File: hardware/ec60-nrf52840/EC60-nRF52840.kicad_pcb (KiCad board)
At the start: 4 copper layers, 285 x 94.6 mm, 180 parts, among them J1 REAR_USB_DAUGHTERBOARD, J2 PROTECTED_1S_4V2_NTC10K, J3 SWD_POGO, SW1 EVQPUC02K_RESET, SW10 EC_SW, SW100 JS102011SAQN_POWER, SW11 EC_SW, SW12 EC_SW, SW13 EC_SW, SW14 EC_SW, SW15 EC_SW, SW16 EC_SW, SW17 EC_SW, SW18 EC_SW, SW19 EC_SW, SW2 EC_SW, SW20 EC_SW, SW21 EC_SW, SW22 EC_SW, SW23 EC_SW, SW24 EC_SW, SW25 EC_SW, SW26 EC_SW, SW27 EC_SW, SW28 EC_SW, SW29 EC_SW, SW3 EC_SW, SW30 EC_SW, SW31 ANSI_\, SW32 ISO_Enter, SW33 EC_SW, SW34 EC_SW, SW35 EC_SW, SW36 EC_SW, SW37 EC_SW, SW38 EC_SW, SW39 EC_SW, SW4 EC_SW, SW40 EC_SW, SW41 EC_SW, SW42 EC_SW, SW43 EC_SW, SW44 EC_SW, SW45 ISO_|, SW46 ANSI_Enter, SW47 EC_SW, SW48 EC_SW, SW49 EC_SW, SW5 EC_SW, SW50 EC_SW, SW51 EC_SW, SW52 EC_SW, SW53 EC_SW, SW54 EC_SW, SW55 EC_SW, SW56 EC_SW, SW57 EC_SW, SW58 EC_SW, SW59 EC_SW, SW6 EC_SW, SW60 EC_SW_1u&1.75u, SW61 EC_SW, SW62 EC_SW_1u&1.75u, SW63 EC_SW, SW64 EC_SW, SW65 EC_SW, SW66 EC_SW, SW67 EC_SW, SW68 EC_SW, SW69 EC_SW, SW7 EC_SW, SW70 EC_SW, SW71 EC_SW, SW72 EC_SW, SW73 EC_SW, SW74 EC_SW, SW75 EC_SW, SW8 EC_SW, SW9 EC_SW, U1 MDBT50Q-1MV2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

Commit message: fix: validate single-nRF PCB and add 3D renders
Complete routing and native clearance repairs, freeze footprint metadata, and preserve EC60 sensing and mounting geometry. Add reproducible KiCad stills and a six-second 3D turntable with model provenance.

Validation: strict DRC 0 errors and 0 opens; ERC 0 errors; 268 physical pin pairs pass with no connectivity regressions. Render source hashes are unchanged, and MP4/GIF decoding passes. Physical assembly and SI/RF validation remain pending.
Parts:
- removed G*** (x3): LOGO, LOGO
- C10: footprint Capacitor_SMD:C_0402_1005Metric -> YAECKB:C_0402_1005Metric__C10
- C11: footprint Capacitor_SMD:C_0402_1005Metric -> YAECKB:C_0402_1005Metric__C11
- C12: footprint Capacitor_SMD:C_0402_1005Metric -> YAECKB:C_0402_1005Metric__C12
- C13: footprint Capacitor_SMD:C_0402_1005Metric -> YAECKB:C_0402_1005Metric__C13
- C30: footprint Capacitor_SMD:C_0603_1608Metric -> YAECKB:C_0603_1608Metric__C30
- C31: footprint Capacitor_SMD:C_0402_1005Metric -> YAECKB:C_0402_1005Metric__C31
- C32: footprint Capacitor_SMD:C_0603_1608Metric -> YAECKB:C_0603_1608Metric__C32
- C40: footprint Capacitor_SMD:C_0603_1608Metric -> YAECKB:C_0603_1608Metric__C40
- C41: footprint Capacitor_SMD:C_0603_1608Metric -> YAECKB:C_0603_1608Metric__C41
- C42: footprint Capacitor_SMD:C_0603_1608Metric -> YAECKB:C_0603_1608Metric__C42
- C43: footprint Capacitor_SMD:C_0603_1608Metric -> YAECKB:C_0603_1608Metric__C43
- C44: footprint Capacitor_SMD:C_0603_1608Metric -> YAECKB:C_0603_1608Metric__C44
- C45: footprint Capacitor_SMD:C_0603_1608Metric -> YAECKB:C_0603_1608Metric__C45
- C46: footprint Capacitor_SMD:C_0603_1608Metric -> YAECKB:C_0603_1608Metric__C46
- C47: footprint Capacitor_SMD:C_0402_1005Metric -> YAECKB:C_0402_1005Metric__C47
- C48: footprint Capacitor_SMD:C_0402_1005Metric -> YAECKB:C_0402_1005Metric__C48
- C9: footprint Capacitor_SMD:C_0402_1005Metric -> YAECKB:C_0402_1005Metric__C9
- D1: footprint Package_TO_SOT_SMD:SOT-143 -> YAECKB:SOT-143__D1
- D2: footprint LED_SMD:LED_0603_1608Metric -> YAECKB:LED_0603_1608Metric__D2
- F1: footprint Fuse:Fuse_1206_3216Metric -> YAECKB:Fuse_1206_3216Metric__F1
- H1: footprint YAECKB:HOLE_M2 -> YAECKB:HOLE_M2__H1
- H10: footprint YAECKB:HOLE_M2 -> YAECKB:HOLE_M2__H10
- H11: footprint YAECKB:HOLE_M2 -> YAECKB:HOLE_M2__H11
- H12: footprint YAECKB:HOLE_M2 -> YAECKB:HOLE_M2__H12
- H13: footprint YAECKB:HOLE_M2 -> YAECKB:HOLE_M2__H13
- H14: footprint YAECKB:HOLE_M2 -> YAECKB:HOLE_M2__H14
- H15: footprint YAECKB:HOLE_M2 -> YAECKB:HOLE_M2__H15
- H16: footprint YAECKB:HOLE_M2 -> YAECKB:HOLE_M2__H16
- H17: footprint YAECKB:HOLE_M2 -> YAECKB:HOLE_M2__H17
- H18: footprint YAECKB:HOLE_M2 -> YAECKB:HOLE_M2__H18
- H19: footprint YAECKB:HOLE_M2 -> YAECKB:HOLE_M2__H19
- H2: footprint YAECKB:HOLE_M2 -> YAECKB:HOLE_M2__H2
- H20: footprint YAECKB:HOLE_M2 -> YAECKB:HOLE_M2__H20
- H21: footprint YAECKB:HOLE_M2 -> YAECKB:HOLE_M2__H21
- H22: footprint YAECKB:HOLE_M2 -> YAECKB:HOLE_M2__H22
- H23: footprint YAECKB:HOLE_M2 -> YAECKB:HOLE_M2__H23
- H24: footprint YAECKB:HOLE_M2 -> YAECKB:HOLE_M2__H24
- H25: footprint YAECKB:HOLE_M2 -> YAECKB:HOLE_M2__H25
- H26: footprint YAECKB:HOLE_M2 -> YAECKB:HOLE_M2__H26
- H3: footprint YAECKB:HOLE_M2 -> YAECKB:HOLE_M2__H3
- H4: footprint YAECKB:HOLE_M2 -> YAECKB:HOLE_M2__H4
- H5: footprint YAECKB:HOLE_M2 -> YAECKB:HOLE_M2__H5
- H6: footprint YAECKB:HOLE_M2 -> YAECKB:HOLE_M2__H6
- H7: footprint YAECKB:HOLE_M2 -> YAECKB:HOLE_M2__H7
- H8: footprint YAECKB:HOLE_M2 -> YAECKB:HOLE_M2__H8
- H9: footprint YAECKB:HOLE_M2 -> YAECKB:HOLE_M2__H9
- J1: footprint YAECKB:JST-SR-4 -> YAECKB:JST-SR-4__J1
- J2: footprint Connector_JST:JST_PH_S3B-PH-SM4-TB_1x03-1MP_P2.00mm_Horizontal -> YAECKB:JST_PH_S3B-PH-SM4-TB_1x03-1MP_P2.00mm_Horizontal__J2
- J3: footprint YAECKB:SWD_Pogo_2x03 -> YAECKB:SWD_Pogo_2x03__J3
- JP1: footprint Resistor_SMD:R_0603_1608Metric_Pad0.98x0.95mm_HandSolder -> YAECKB:R_0603_1608Metric_Pad0.98x0.95mm_HandSolder__JP1
- L1: footprint Inductor_SMD:L_Wuerth_MAPI-3015 -> YAECKB:L_Wuerth_MAPI-3015__L1
- R10: footprint Resistor_SMD:R_0402_1005Metric -> YAECKB:R_0402_1005Metric__R10
- R11: footprint Resistor_SMD:R_0402_1005Metric -> YAECKB:R_0402_1005Metric__R11
- R12: footprint Resistor_SMD:R_0402_1005Metric -> YAECKB:R_0402_1005Metric__R12
- R13: footprint Resistor_SMD:R_0402_1005Metric -> YAECKB:R_0402_1005Metric__R13
- R14: footprint Resistor_SMD:R_0402_1005Metric -> YAECKB:R_0402_1005Metric__R14
- R15: footprint Resistor_SMD:R_0402_1005Metric -> YAECKB:R_0402_1005Metric__R15
- R16: footprint Resistor_SMD:R_0402_1005Metric -> YAECKB:R_0402_1005Metric__R16
- R17: footprint Resistor_SMD:R_0402_1005Metric -> YAECKB:R_0402_1005Metric__R17
- R18: footprint Resistor_SMD:R_0402_1005Metric -> YAECKB:R_0402_1005Metric__R18
- R19: footprint Resistor_SMD:R_0402_1005Metric -> YAECKB:R_0402_1005Metric__R19
- R20: footprint Resistor_SMD:R_0402_1005Metric -> YAECKB:R_0402_1005Metric__R20
- R21: footprint Resistor_SMD:R_0402_1005Metric -> YAECKB:R_0402_1005Metric__R21
- R23: footprint Resistor_SMD:R_0402_1005Metric -> YAECKB:R_0402_1005Metric__R23
- R24: footprint Resistor_SMD:R_0402_1005Metric -> YAECKB:R_0402_1005Metric__R24
- R25: footprint Resistor_SMD:R_0402_1005Metric -> YAECKB:R_0402_1005Metric__R25
- R26: footprint Resistor_SMD:R_0402_1005Metric -> YAECKB:R_0402_1005Metric__R26
- R3: footprint Resistor_SMD:R_0402_1005Metric -> YAECKB:R_0402_1005Metric__R3
- R30: footprint Resistor_SMD:R_0402_1005Metric -> YAECKB:R_0402_1005Metric__R30
- R31: footprint Resistor_SMD:R_0402_1005Metric -> YAECKB:R_0402_1005Metric__R31
- R32: footprint Resistor_SMD:R_0402_1005Metric -> YAECKB:R_0402_1005Metric__R32
- R4: footprint Resistor_SMD:R_0402_1005Metric -> YAECKB:R_0402_1005Metric__R4
- R40: footprint Resistor_SMD:R_0402_1005Metric -> YAECKB:R_0402_1005Metric__R40
- R41: footprint Resistor_SMD:R_0402_1005Metric -> YAECKB:R_0402_1005Metric__R41
- R42: footprint Resistor_SMD:R_0402_1005Metric -> YAECKB:R_0402_1005Metric__R42
- R43: footprint Resistor_SMD:R_0402_1005Metric -> YAECKB:R_0402_1005Metric__R43
- R44: footprint Resistor_SMD:R_0402_1005Metric -> YAECKB:R_0402_1005Metric__R44
- R45: footprint Resistor_SMD:R_0402_1005Metric -> YAECKB:R_0402_1005Metric__R45
- R46: footprint Resistor_SMD:R_0402_1005Metric -> YAECKB:R_0402_1005Metric__R46
- R47: footprint Resistor_SMD:R_0402_1005Metric -> YAECKB:R_0402_1005Metric__R47
- R48: footprint Resistor_SMD:R_0402_1005Metric -> YAECKB:R_0402_1005Metric__R48
- R49: footprint Resistor_SMD:R_0402_1005Metric -> YAECKB:R_0402_1005Metric__R49
- R5: footprint Resistor_SMD:R_0402_1005Metric -> YAECKB:R_0402_1005Metric__R5
- R50: footprint Resistor_SMD:R_0402_1005Metric -> YAECKB:R_0402_1005Metric__R50
- R51: footprint Resistor_SMD:R_0402_1005Metric -> YAECKB:R_0402_1005Metric__R51
- R52: footprint Resistor_SMD:R_0402_1005Metric -> YAECKB:R_0402_1005Metric__R52
- R53: footprint Resistor_SMD:R_0402_1005Metric -> YAECKB:R_0402_1005Metric__R53
- R54: footprint Resistor_SMD:R_0402_1005Metric -> YAECKB:R_0402_1005Metric__R54
- R6: footprint Resistor_SMD:R_0402_1005Metric -> YAECKB:R_0402_1005Metric__R6
- R7: footprint Resistor_SMD:R_0402_1005Metric -> YAECKB:R_0402_1005Metric__R7
- R8: footprint Resistor_SMD:R_0402_1005Metric -> YAECKB:R_0402_1005Metric__R8
- R9: footprint Resistor_SMD:R_0402_1005Metric -> YAECKB:R_0402_1005Metric__R9
- REF**: footprint locallib:60_Outline-Modded-Extreme -> YAECKB:EC60_BoardOutline__REF__
- SW1: footprint Button_Switch_SMD:Panasonic_EVQPUL_EVQPUC -> YAECKB:Panasonic_EVQPUL_EVQPUC__SW1
- SW10: footprint YAECKB:ecs_pad_no_ring -> YAECKB:ecs_pad_no_ring__SW10
- SW100: footprint Button_Switch_SMD:SW_SPDT_CK_JS102011SAQN -> YAECKB:SW_SPDT_CK_JS102011SAQN__SW100
- SW11: footprint YAECKB:ecs_pad_no_ring -> YAECKB:ecs_pad_no_ring__SW11
- SW12: footprint YAECKB:ecs_pad_no_ring -> YAECKB:ecs_pad_no_ring__SW12
- SW13: footprint YAECKB:ecs_pad_no_ring -> YAECKB:ecs_pad_no_ring__SW13
- SW14: footprint YAECKB:ecs_pad_no_ring -> YAECKB:ecs_pad_no_ring__SW14
- SW15: footprint YAECKB:ecs_pad_no_ring -> YAECKB:ecs_pad_no_ring__SW15
- SW16: footprint YAECKB:ecs_pad_no_ring -> YAECKB:ecs_pad_no_ring__SW16
- SW17: footprint YAECKB:ecs_pad_no_ring -> YAECKB:ecs_pad_no_ring__SW17
- SW18: footprint YAECKB:ecs_pad_no_ring -> YAECKB:ecs_pad_no_ring__SW18
- SW19: footprint YAECKB:ecs_pad_no_ring -> YAECKB:ecs_pad_no_ring__SW19
- SW2: footprint YAECKB:ecs_pad_no_ring -> YAECKB:ecs_pad_no_ring__SW2
- SW20: footprint YAECKB:ecs_pad_no_ring -> YAECKB:ecs_pad_no_ring__SW20
- SW21: footprint YAECKB:ecs_pad_no_ring -> YAECKB:ecs_pad_no_ring__SW21
- SW22: footprint YAECKB:ecs_pad_no_ring -> YAECKB:ecs_pad_no_ring__SW22
- SW23: footprint YAECKB:ecs_pad_no_ring -> YAECKB:ecs_pad_no_ring__SW23
- SW24: footprint YAECKB:ecs_pad_no_ring -> YAECKB:ecs_pad_no_ring__SW24
- SW25: footprint YAECKB:ecs_pad_no_ring -> YAECKB:ecs_pad_no_ring__SW25
- SW26: footprint YAECKB:ecs_pad_no_ring -> YAECKB:ecs_pad_no_ring__SW26
- SW27: footprint YAECKB:ecs_pad_no_ring -> YAECKB:ecs_pad_no_ring__SW27
- SW28: footprint YAECKB:ecs_pad_no_ring -> YAECKB:ecs_pad_no_ring__SW28
- SW29: footprint YAECKB:ecs_pad_no_ring -> YAECKB:ecs_pad_no_ring__SW29
- SW3: footprint YAECKB:ecs_pad_no_ring -> YAECKB:ecs_pad_no_ring__SW3
- SW30: footprint YAECKB:ecs_pad_no_ring -> YAECKB:ecs_pad_no_ring__SW30
- SW31: footprint YAECKB:ecs_pad_no_ring -> YAECKB:ecs_pad_no_ring__SW31
- SW32: footprint YAECKB:ecs_pad_no_ring -> YAECKB:ecs_pad_no_ring__SW32
- SW33: footprint YAECKB:ecs_pad_no_ring_stepped&normal -> YAECKB:ecs_pad_no_ring_stepped&normal__SW33
- SW34: footprint YAECKB:ecs_pad_no_ring -> YAECKB:ecs_pad_no_ring__SW34
- SW35: footprint YAECKB:ecs_pad_no_ring -> YAECKB:ecs_pad_no_ring__SW35
- SW36: footprint YAECKB:ecs_pad_no_ring -> YAECKB:ecs_pad_no_ring__SW36
- SW37: footprint YAECKB:ecs_pad_no_ring -> YAECKB:ecs_pad_no_ring__SW37
- SW38: footprint YAECKB:ecs_pad_no_ring -> YAECKB:ecs_pad_no_ring__SW38
- SW39: footprint YAECKB:ecs_pad_no_ring -> YAECKB:ecs_pad_no_ring__SW39
- SW4: footprint YAECKB:ecs_pad_no_ring -> YAECKB:ecs_pad_no_ring__SW4
- SW40: footprint YAECKB:ecs_pad_no_ring -> YAECKB:ecs_pad_no_ring__SW40
- SW41: footprint YAECKB:ecs_pad_no_ring -> YAECKB:ecs_pad_no_ring__SW41
- SW42: footprint YAECKB:ecs_pad_no_ring -> YAECKB:ecs_pad_no_ring__SW42
- SW43: footprint YAECKB:ecs_pad_no_ring -> YAECKB:ecs_pad_no_ring__SW43
- SW44: footprint YAECKB:ecs_pad_no_ring -> YAECKB:ecs_pad_no_ring__SW44
- SW45: footprint YAECKB:ecs_pad_no_ring -> YAECKB:ecs_pad_no_ring__SW45
- SW46: footprint YAECKB:ecs_pad_no_ring -> YAECKB:ecs_pad_no_ring__SW46
- SW47: footprint YAECKB:ecs_pad_no_ring -> YAECKB:ecs_pad_no_ring__SW47
- SW48: footprint YAECKB:ecs_pad_no_ring_1u_edge_cut -> YAECKB:ecs_pad_no_ring_1u_edge_cut__SW48
- SW49: footprint YAECKB:ecs_pad_no_ring_1u_edge_cut -> YAECKB:ecs_pad_no_ring_1u_edge_cut__SW49
- SW5: footprint YAECKB:ecs_pad_no_ring -> YAECKB:ecs_pad_no_ring__SW5
- SW50: footprint YAECKB:ecs_pad_no_ring -> YAECKB:ecs_pad_no_ring__SW50
- SW51: footprint YAECKB:ecs_pad_no_ring -> YAECKB:ecs_pad_no_ring__SW51
- SW52: footprint YAECKB:ecs_pad_no_ring -> YAECKB:ecs_pad_no_ring__SW52
- SW53: footprint YAECKB:ecs_pad_no_ring -> YAECKB:ecs_pad_no_ring__SW53
- SW54: footprint YAECKB:ecs_pad_no_ring -> YAECKB:ecs_pad_no_ring__SW54
- SW55: footprint YAECKB:ecs_pad_no_ring -> YAECKB:ecs_pad_no_ring__SW55
- SW56: footprint YAECKB:ecs_pad_no_ring -> YAECKB:ecs_pad_no_ring__SW56
- SW57: footprint YAECKB:ecs_pad_no_ring -> YAECKB:ecs_pad_no_ring__SW57
- SW58: footprint YAECKB:ecs_pad_no_ring -> YAECKB:ecs_pad_no_ring__SW58
- SW59: footprint YAECKB:ecs_pad_no_ring -> YAECKB:ecs_pad_no_ring__SW59
- SW6: footprint YAECKB:ecs_pad_no_ring -> YAECKB:ecs_pad_no_ring__SW6
- SW60: footprint YAECKB:ecs_pad_no_ring_1u1.75u -> YAECKB:ecs_pad_no_ring_1u1.75u__SW60
- SW61: footprint YAECKB:ecs_pad_no_ring -> YAECKB:ecs_pad_no_ring__SW61
- SW62: footprint YAECKB:ecs_pad_no_ring_1u1.75u -> YAECKB:ecs_pad_no_ring_1u1.75u__SW62
- SW63: footprint YAECKB:ecs_pad_no_ring -> YAECKB:ecs_pad_no_ring__SW63
- SW64: footprint YAECKB:ecs_pad_no_ring -> YAECKB:ecs_pad_no_ring__SW64
- SW65: footprint YAECKB:ecs_pad_no_ring -> YAECKB:ecs_pad_no_ring__SW65
- SW66: footprint YAECKB:ecs_pad_no_ring -> YAECKB:ecs_pad_no_ring__SW66
- SW67: footprint YAECKB:ecs_pad_no_ring -> YAECKB:ecs_pad_no_ring__SW67
- SW68: footprint YAECKB:ecs_pad_no_ring_stepped&normal -> YAECKB:ecs_pad_no_ring_stepped&normal__SW68
- SW69: footprint YAECKB:ecs_pad_no_ring_stepped&normal -> YAECKB:ecs_pad_no_ring_stepped&normal__SW69
- SW7: footprint YAECKB:ecs_pad_no_ring -> YAECKB:ecs_pad_no_ring__SW7
- SW70: footprint YAECKB:ecs_pad_no_ring -> YAECKB:ecs_pad_no_ring__SW70
- SW71: footprint YAECKB:ecs_pad_no_ring_stepped&normal -> YAECKB:ecs_pad_no_ring_stepped&normal__SW71
- SW72: footprint YAECKB:ecs_pad_no_ring -> YAECKB:ecs_pad_no_ring__SW72
- SW73: footprint YAECKB:ecs_pad_no_ring -> YAECKB:ecs_pad_no_ring__SW73
- SW74: footprint YAECKB:ecs_pad_no_ring -> YAECKB:ecs_pad_no_ring__SW74
- SW75: footprint YAECKB:ecs_pad_no_ring -> YAECKB:ecs_pad_no_ring__SW75
- SW8: footprint YAECKB:ecs_pad_no_ring -> YAECKB:ecs_pad_no_ring__SW8
- SW9: footprint YAECKB:ecs_pad_no_ring -> YAECKB:ecs_pad_no_ring__SW9
- U1: footprint RF_Module:Raytac_MDBT50Q -> YAECKB:Raytac_MDBT50Q__U1
- U2: footprint YAECKB:TSSOP16 -> YAECKB:TSSOP16__U2
- U3: footprint Package_SO:SOIC-8_3.9x4.9mm_P1.27mm -> YAECKB:SOIC-8_3.9x4.9mm_P1.27mm__U3
- U4: footprint YAECKB:TSSOP16 -> YAECKB:TSSOP16__U4
- U5: footprint Package_DFN_QFN:VQFN-16-1EP_3x3mm_P0.5mm_EP1.6x1.6mm -> YAECKB:VQFN-16-1EP_3x3mm_P0.5mm_EP1.6x1.6mm__U5
- U6: footprint Package_SON:WSON-10-1EP_2.5x2.5mm_P0.5mm_EP1.2x2mm -> YAECKB:WSON-10-1EP_2.5x2.5mm_P0.5mm_EP1.2x2mm__U6
- U7: footprint Package_TO_SOT_SMD:SOT-363_SC-70-6 -> YAECKB:SOT-363_SC-70-6__U7
- U8: footprint Package_TO_SOT_SMD:SOT-363_SC-70-6 -> YAECKB:SOT-363_SC-70-6__U8
- moved R40 7.21 mm to (117.2, 148.1), turned to -90 degrees
- moved C40 2.50 mm to (118.0, 151.0)
- turned L1 to -90 degrees
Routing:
- net ROW_DRV0: track 29.1 -> 291.2 mm, vias 1 -> 4
- net ROW_DRV4: track 11.9 -> 270.0 mm, vias 1 -> 5
- net ROW_DRV2: track 7.85 -> 265.2 mm, vias 0 -> 9
- net ROW_DRV3: track 8.22 -> 265.4 mm, vias 1 -> 7
- net ROW_DRV1: track 9.04 -> 264.6 mm, vias 1 -> 3
- net ADC: track 21.3 -> 260.5 mm, vias 1 -> 2
- net PGOOD_N: track 1.90 -> 239.7 mm, vias 2 -> 5
- net USB_5V: track 67.4 -> 301.1 mm, vias 2 -> 9
- net APLEX_EN_PIN_1: track 311.5 -> 116.0 mm, vias 5 -> 2
- net D-: track 74.8 -> 262.8 mm, vias 3 -> 6
- net AFE_3V3: track 81.2 -> 256.7 mm
- net AMUX_SEL_0: track 471.0 -> 305.6 mm, vias 9 -> 5
- net BAT_NTC: track 3.58 -> 57.3 mm, vias 1 -> 4
- net APLEX_OUT_PIN_0: track 274.5 -> 311.6 mm, vias 1 -> 2
- net D+: track 290.3 -> 253.7 mm
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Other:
- board text added: "NRF-1.0-dev / REAR USB"
- board text added: "YAECKB / EC60 by Cipulot"

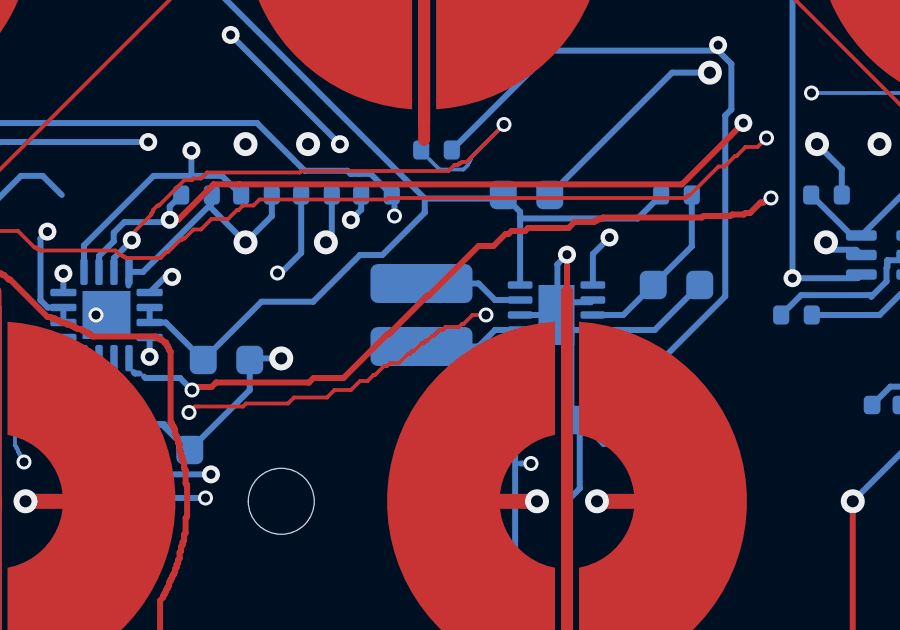
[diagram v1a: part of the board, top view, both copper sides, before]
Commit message: feat: checkpoint YETI60 electrical review and firmware simulation
Replace inherited USB series resistance with 0R links for the nRF52840 PHY. Add a schematic-derived pin contract, portable scan/power/HID control core and ASan/UBSan host simulation. Begin YETI60 branding and English/Chinese documentation migration.

CAD: zero strict DRC errors, zero opens and all 268 physical pin pairs pass. Host simulation passes; real peripherals and transport stacks remain mocked. Power-route optimization, assembly Z fit, battery-space study, assembled renders and remaining bilingual documents continue after this checkpoint.
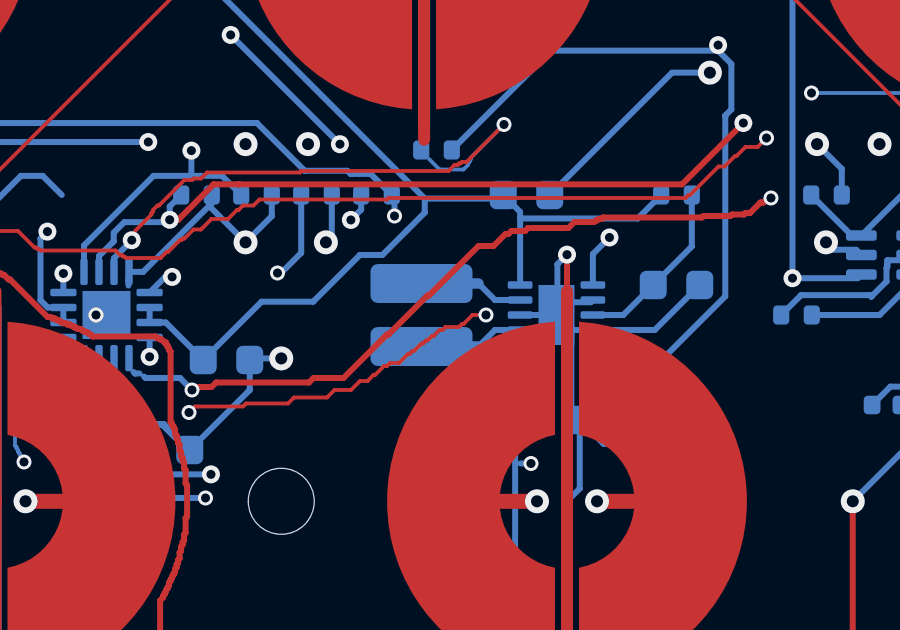
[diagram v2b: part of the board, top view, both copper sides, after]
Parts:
- R30, R31: value 27 -> 0
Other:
- board text added: "YETI60 / EC60 by Cipulot"
- board text removed: "YAECKB / EC60 by Cipulot"
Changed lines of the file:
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@@
 			)
 		)
-		(property "Value" "27"
+		(property "Value" "0"
 			(at 0 -1.17 180)
 			(layer "B.Fab")
@@
 			)
 		)
-		(property "Value" "27"
+		(property "Value" "0"
 			(at 0 -1.17 180)
 			(layer "B.Fab")
@@
 		(layer "B.Fab")
 	)
-	(gr_text "YAECKB / EC60 by Cipulot"
+	(gr_text "YETI60 / EC60 by Cipulot"
 		(at 214 141.5 0)
 		(layer "B.SilkS")
@@
 		(start 128.5 143.95)
 		(end 130.4 143.95)
-		(width 0.2)
+		(width 0.35)
 		(layer "B.Cu")
 		(net "BUCK_L1")
@@
 		(start 128.5 146.05)
 		(end 130.4 146.05)
-		(width 0.2)
+		(width 0.35)
 		(layer "B.Cu")
 		(net "BUCK_L2")
